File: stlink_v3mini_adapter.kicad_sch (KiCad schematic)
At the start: 34 parts, among them J1 Conn_02x07_Odd_Even, J2 Conn_02x05_Odd_Even, J3 Conn_01x05_Pin, SW1 RST, U3 TLV71333PDBV

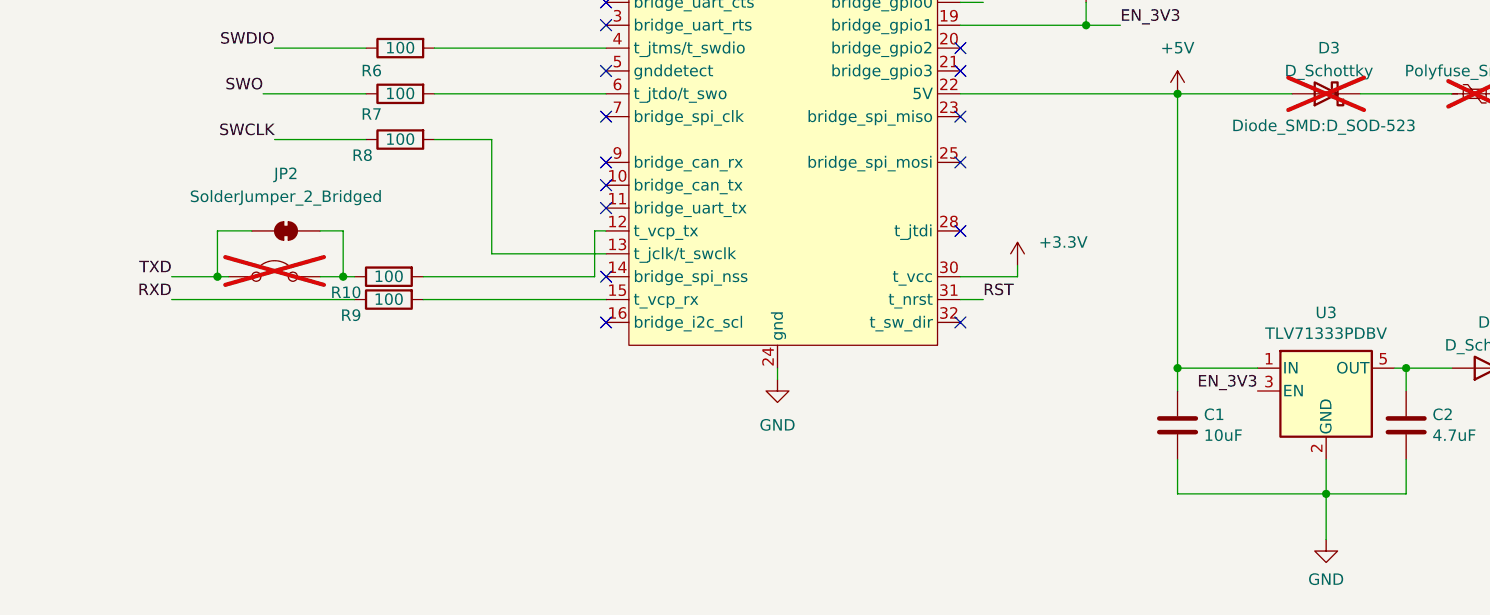
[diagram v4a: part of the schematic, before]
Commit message: 1.2.1: actually cut RX instead of TX..
Signed-off-by: Guillaume Revaillot <guillaume.revaillot@wirestone.io>
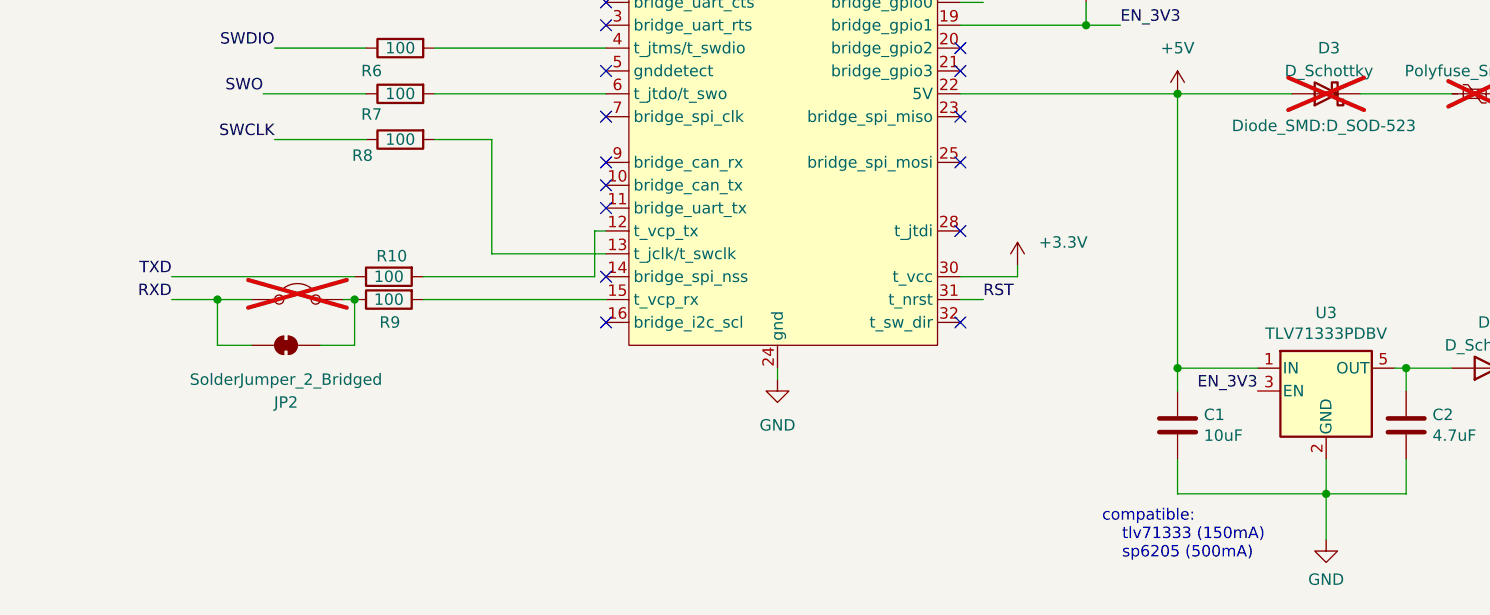
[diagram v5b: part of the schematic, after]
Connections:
- net RXD: now also JP1.2 (B), JP2.2 (B); no longer R9.1
- net TXD: now also R10.1; no longer JP1.2 (B), JP2.1 (A)
- new net: JP1.1 (A), JP2.1 (A), R9.1
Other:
- note added: "compatible: tlv71333 (150mA) sp6205 (500mA)"
- moved on the sheet: JP2
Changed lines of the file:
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@@
 	(title_block
 		(title "stlinkv3mods wirestone adapter")
-		(date "2023-06-26")
-		(rev "1.1.0")
+		(date "2024-11-25")
+		(rev "1.2.1")
 	)
 	(junction
@@
 	)
 	(junction
+		(at 46.99 113.03)
+		(diameter 0)
+		(color 0 0 0 0)
+	)
+	(junction
 		(at 220.98 120.65)
 		(diameter 0)
@@
 	)
 	(junction
-		(at 46.99 110.49)
+		(at 215.9 54.61)
 		(diameter 0)
 		(color 0 0 0 0)
 	)
 	(junction
-		(at 215.9 54.61)
+		(at 62.23 113.03)
 		(diameter 0)
 		(color 0 0 0 0)
@@
 		(color 0 0 0 0)
 	)
-	(junction
-		(at 60.96 110.49)
-		(diameter 0)
-		(color 0 0 0 0)
-	)
 	(no_connect
 		(at 80.01 60.96)
@@
 	(wire
 		(pts
-			(xy 46.99 105.41) (xy 46.99 110.49)
+			(xy 62.23 118.11) (xy 62.23 113.03)
 		)
 		(stroke
@@
 	(wire
 		(pts
-			(xy 41.91 110.49) (xy 46.99 110.49)
+			(xy 41.91 110.49) (xy 62.23 110.49)
 		)
 		(stroke
@@
 	(wire
 		(pts
-			(xy 60.96 105.41) (xy 60.96 110.49)
+			(xy 168.91 67.31) (xy 168.91 72.39)
 		)
 		(stroke
@@
 	(wire
 		(pts
-			(xy 168.91 67.31) (xy 168.91 72.39)
+			(xy 129.54 110.49) (xy 135.89 110.49)
 		)
 		(stroke
@@
 	(wire
 		(pts
-			(xy 129.54 110.49) (xy 135.89 110.49)
+			(xy 203.2 54.61) (xy 209.55 54.61)
 		)
 		(stroke
@@
 	(wire
 		(pts
-			(xy 203.2 54.61) (xy 209.55 54.61)
+			(xy 52.07 50.8) (xy 52.07 55.88)
 		)
 		(stroke
@@
 	(wire
 		(pts
-			(xy 52.07 50.8) (xy 52.07 55.88)
+			(xy 196.85 90.17) (xy 198.12 90.17)
 		)
 		(stroke
@@
 	(wire
 		(pts
-			(xy 58.42 110.49) (xy 60.96 110.49)
+			(xy 184.15 90.17) (xy 173.99 90.17)
 		)
 		(stroke
@@
 	(wire
 		(pts
-			(xy 196.85 90.17) (xy 198.12 90.17)
+			(xy 191.77 120.65) (xy 194.31 120.65)
 		)
 		(stroke
@@
 	(wire
 		(pts
-			(xy 184.15 90.17) (xy 173.99 90.17)
+			(xy 60.96 48.26) (xy 67.31 48.26)
 		)
 		(stroke
@@
 	(wire
 		(pts
-			(xy 191.77 120.65) (xy 194.31 120.65)
+			(xy 80.01 48.26) (xy 101.6 48.26)
 		)
 		(stroke
@@
 	(wire
 		(pts
-			(xy 60.96 48.26) (xy 67.31 48.26)
+			(xy 224.79 139.7) (xy 224.79 137.16)
 		)
 		(stroke
@@
 	(wire
 		(pts
-			(xy 80.01 48.26) (xy 101.6 48.26)
+			(xy 71.12 90.17) (xy 90.17 90.17)
 		)
 		(stroke
@@
 	(wire
 		(pts
-			(xy 224.79 139.7) (xy 224.79 137.16)
+			(xy 153.67 90.17) (xy 166.37 90.17)
 		)
 		(stroke
@@
 	(wire
 		(pts
-			(xy 71.12 90.17) (xy 90.17 90.17)
+			(xy 41.91 113.03) (xy 46.99 113.03)
 		)
 		(stroke
@@
 	(wire
 		(pts
-			(xy 153.67 90.17) (xy 166.37 90.17)
+			(xy 109.22 120.65) (xy 109.22 121.92)
 		)
 		(stroke
@@
 	(wire
 		(pts
-			(xy 109.22 120.65) (xy 109.22 121.92)
+			(xy 46.99 118.11) (xy 46.99 113.03)
 		)
 		(stroke
@@
 	(wire
 		(pts
-			(xy 196.85 90.17) (xy 189.23 90.17)
+			(xy 46.99 118.11) (xy 50.8 118.11)
 		)
 		(stroke
@@
 	(wire
 		(pts
-			(xy 46.99 105.41) (xy 50.8 105.41)
+			(xy 196.85 90.17) (xy 189.23 90.17)
 		)
 		(stroke
@@
 	(wire
 		(pts
-			(xy 58.42 105.41) (xy 60.96 105.41)
+			(xy 62.23 118.11) (xy 58.42 118.11)
 		)
 		(stroke
@@
 	(wire
 		(pts
-			(xy 48.26 110.49) (xy 46.99 110.49)
-		)
-		(stroke
-			(width 0)
-			(type default)
-		)
-	)
-	(wire
-		(pts
 			(xy 205.74 90.17) (xy 207.01 90.17)
 		)
@@
 	(wire
 		(pts
+			(xy 46.99 113.03) (xy 50.8 113.03)
+		)
+		(stroke
+			(width 0)
+			(type default)
+		)
+	)
+	(wire
+		(pts
 			(xy 77.47 95.25) (xy 77.47 107.95)
 		)
@@
 	(wire
 		(pts
-			(xy 60.96 110.49) (xy 62.23 110.49)
-		)
-		(stroke
-			(width 0)
-			(type default)
-		)
-	)
-	(wire
-		(pts
-			(xy 41.91 113.03) (xy 62.23 113.03)
+			(xy 60.96 113.03) (xy 62.23 113.03)
 		)
 		(stroke
@@
 		)
 	)
+	(text "compatible:\n	tlv71333 (150mA)\n	sp6205 (500mA)"
+		(exclude_from_sim no)
+		(at 145.288 139.192 0)
+		(effects
+			(font
+				(size 1.27 1.27)
+			)
+			(justify left)
+		)
+	)
 	(label "SWO"
 		(at 52.07 90.17 180)
@@
 		(dnp no)
 		(property "Reference" "R10"
-			(at 62.992 112.268 90)
+			(at 68.072 108.204 90)
 			(effects
 				(font
@@
 		(lib_name "Jumper_2_Open_1")
 		(lib_id "Jumper:Jumper_2_Open")
-		(at 53.34 110.49 0)
+		(at 55.88 113.03 0)
 		(mirror y)
 		(unit 1)
@@
 		(dnp yes)
 		(property "Reference" "JP1"
-			(at 12.7 114.3 0)
+			(at 15.24 116.84 0)
 			(effects
 				(font
@@
 		)
 		(property "Value" "Jumper_2_Open"
-			(at 53.34 107.95 0)
+			(at 55.88 110.49 0)
 			(effects
 				(font
@@
 		)
 		(property "Footprint" "Connector_PinSocket_2.54mm:PinSocket_1x02_P2.54mm_Vertical"
-			(at 53.34 110.49 0)
+			(at 55.88 113.03 0)
 			(effects
 				(font
@@
 		)
 		(property "Datasheet" "~"
-			(at 53.34 110.49 0)
+			(at 55.88 113.03 0)
 			(effects
 				(font
@@
 		)
 		(property "Description" "Jumper, 2-pole, open"
-			(at 53.34 110.49 0)
+			(at 55.88 113.03 0)
 			(effects
 				(font
@@
 		(dnp no)
 		(property "Reference" "R9"
-			(at 62.992 114.808 90)
+			(at 67.31 115.57 90)
 			(effects
 				(font
@@
 	(symbol
 		(lib_id "Jumper:SolderJumper_2_Bridged")
-		(at 54.61 105.41 0)
+		(at 54.61 118.11 180)
 		(unit 1)
 		(exclude_from_sim yes)
@@
 		(fields_autoplaced yes)
 		(property "Reference" "JP2"
-			(at 54.61 99.06 0)
+			(at 54.61 124.46 0)
 			(effects
 				(font
@@
 		)
 		(property "Value" "SolderJumper_2_Bridged"
-			(at 54.61 101.6 0)
+			(at 54.61 121.92 0)
 			(effects
 				(font
@@
 		)
 		(property "Footprint" "Jumper:SolderJumper-2_P1.3mm_Bridged_RoundedPad1.0x1.5mm"
-			(at 54.61 105.41 0)
+			(at 54.61 118.11 0)
 			(effects
 				(font
@@
 		)
 		(property "Datasheet" "~"
-			(at 54.61 105.41 0)
+			(at 54.61 118.11 0)
 			(effects
 				(font
@@
 		)
 		(property "Description" "Solder Jumper, 2-pole, closed/bridged"
-			(at 54.61 105.41 0)
+			(at 54.61 118.11 0)
 			(effects
 				(font
